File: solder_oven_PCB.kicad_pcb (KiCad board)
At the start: 2 copper layers, 4 parts

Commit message: update: now the pcb has sheets and pcb layout
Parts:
- added B1: ~, JuanDavid_Library:SW-SMD_L3.9-W2.9-LS4.8, F.Cu at (127.1, 104.0)
- added B2: ~, JuanDavid_Library:SW-SMD_L3.9-W2.9-LS4.8, B.Cu at (127.5, 70.9)
- added C1: 100nF, Capacitor_SMD:C_0805_2012Metric, F.Cu at (90.0, 62.3)
- added C2: 1000uF, Capacitor_THT:CP_Radial_D10.0mm_P3.80mm, F.Cu at (142.9, 48.3)
- added C3: 470uF, Capacitor_SMD:C_Elec_8x6.2, B.Cu at (91.0, 82.9)
- added C4: 220uF, Capacitor_SMD:C_Elec_8x6.2, B.Cu at (117.0, 93.9)
- added C5: 100nF, Capacitor_SMD:C_0603_1608Metric, F.Cu at (130.9, 106.5)
- added C6: 100nF, Capacitor_SMD:C_0603_1608Metric, B.Cu at (131.8, 67.9)
- added C7: 100nF, Capacitor_SMD:C_0805_2012Metric, B.Cu at (123.8, 75.0)
- added D1: Generic_Triac_A1A2G, TerminalBlock:TerminalBlock_Altech_AK300-3_P5.00mm, F.Cu at (146.8, 112.0)
- added D2: LED, LED_THT:LED_D3.0mm, B.Cu at (119.4, 120.5)
- added D3: W10G, Diode_THT:Diode_Bridge_Round_D9.8mm, F.Cu at (135.6, 69.2)
- added D4: LED, LED_THT:LED_D3.0mm, F.Cu at (142.1, 59.7)
- added D5: ~, JuanDavid_Library:SMA_L4.4-W2.8-LS5.4-R-RD, B.Cu at (105.0, 76.9)
- added H1: M3 screw, MountingHole:MountingHole_3.2mm_M3_DIN965_Pad, F.Cu at (80.8, 41.9)
- added H2: M3 screw, MountingHole:MountingHole_3.2mm_M3_DIN965_Pad, F.Cu at (149.6, 42.8)
- added H3: M3 screw, MountingHole:MountingHole_3.2mm_M3_DIN965_Pad, F.Cu at (187.3, 137.2)
- added H4: M3 screw, MountingHole:MountingHole_3.2mm_M3_DIN965_Pad, F.Cu at (82.4, 137.0)
- added J1: UART, Connector_PinSocket_2.54mm:PinSocket_1x03_P2.54mm_Vertical, F.Cu at (106.5, 45.2)
- added L1: ~, JuanDavid_Library:IND-SMD_L10.3-W10.3_1274AS-H-330M, B.Cu at (91.0, 95.9)
- added P1: Conn_WallPlug, TerminalBlock_Phoenix:TerminalBlock_Phoenix_MKDS-1,5-2-5.08_1x02_P5.08mm_Horizontal, F.Cu at (148.2, 93.8)
- added R1: Heater, TerminalBlock_Phoenix:TerminalBlock_Phoenix_MKDS-1,5-2-5.08_1x02_P5.08mm_Horizontal, F.Cu at (147.4, 124.5)
- added R10: 3.3K, Resistor_SMD:R_0603_1608Metric, B.Cu at (131.8, 65.0)
- added R11: 1K, Resistor_THT:R_Axial_DIN0204_L3.6mm_D1.6mm_P5.08mm_Horizontal, B.Cu at (111.8, 115.7)
- added R2: 220, Resistor_THT:R_Axial_DIN0204_L3.6mm_D1.6mm_P5.08mm_Horizontal, B.Cu at (122.9, 115.7)
- added R3: 1K, Resistor_THT:R_Axial_DIN0204_L3.6mm_D1.6mm_P5.08mm_Horizontal, B.Cu at (123.1, 106.2)
- added R4: 1M, Resistor_THT:R_Axial_DIN0204_L3.6mm_D1.6mm_P5.08mm_Horizontal, B.Cu at (106.8, 101.5)
- added R5: 10K, Resistor_THT:R_Axial_DIN0204_L3.6mm_D1.6mm_P5.08mm_Horizontal, B.Cu at (102.8, 113.8)
- added R6: 10K, Resistor_THT:R_Axial_DIN0204_L3.6mm_D1.6mm_P5.08mm_Horizontal, F.Cu at (134.8, 55.7)
- added R7: 10K, Resistor_THT:R_Axial_DIN0204_L3.6mm_D1.6mm_P5.08mm_Horizontal, B.Cu at (112.0, 81.6)
- added R8: 3.3K, Resistor_THT:R_Axial_DIN0204_L3.6mm_D1.6mm_P5.08mm_Horizontal, B.Cu at (116.5, 86.7)
- added R9: 3.3K, Resistor_SMD:R_0603_1608Metric, F.Cu at (130.9, 109.5)
- added T2: ~, JuanDavid_Library:AT-010-V, B.Cu at (138.6, 70.6)
- added TC1: Thermocouple, TerminalBlock_Phoenix:TerminalBlock_Phoenix_MKDS-1,5-2-5.08_1x02_P5.08mm_Horizontal, F.Cu at (147.4, 136.1)
- added U4: H11AA1, Package_DIP:DIP-6_W7.62mm, B.Cu at (114.3, 106.2)
- added U5: MOC3052M, Package_DIP:DIP-6_W7.62mm, B.Cu at (114.3, 120.7)
- added U6: ~, JuanDavid_Library:TO-263-5_L10.2-W8.9-P1.70-BR, B.Cu at (104.0, 87.4)
- added U7: ~, JuanDavid_Library:DIP-16_L20.3-W10.2-P2.54-LS10.2-BL, B.Cu at (93.8, 117.5)
- U3: moved to B.Cu
- moved U2 57.9 mm to (90.8, 68.5), turned to 180 degrees
- moved U1 48.6 mm to (112.2, 61.4)
- moved U3 31.1 mm to (117.2, 76.2)
- moved T1 9.18 mm to (108.5, 133.7)
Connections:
- T1 pad 1: unconnected-(T1-VCC-Pad1) -> +5V
- T1 pad 10: unconnected-(T1-T_CLK-Pad10) -> /esp32/T_CLK
- T1 pad 11: unconnected-(T1-T_CS-Pad11) -> /esp32/T_CS
- T1 pad 12: unconnected-(T1-T_DIN-Pad12) -> /esp32/T_DIN
- T1 pad 13: unconnected-(T1-T_DO-Pad13) -> /esp32/T_DO
- T1 pad 14: unconnected-(T1-T_IRQ-Pad14) -> /esp32/T_IRQ
- T1 pad 2: unconnected-(T1-GND-Pad2) -> GND
- T1 pad 3: unconnected-(T1-CS-Pad3) -> /esp32/CS
- T1 pad 4: unconnected-(T1-RST-Pad4) -> /esp32/RST
- T1 pad 5: unconnected-(T1-DC-Pad5) -> /esp32/D/C
- T1 pad 6: unconnected-(T1-MOSI-Pad6) -> /esp32/MOSI
- T1 pad 7: unconnected-(T1-SCK-Pad7) -> /esp32/CLK
- T1 pad 8: unconnected-(T1-LED-Pad8) -> /esp32/LED
- T1 pad 9: unconnected-(T1-MISO-Pad9) -> /esp32/MISO
- U1 pad 1: Net-(U1-GND-Pad1) -> GND
- U1 pad 10: unconnected-(U1-IO25-Pad10) -> /esp32/T_CLK
- U1 pad 13: unconnected-(U1-IO14-Pad13) -> /esp32/CLK
- U1 pad 14: unconnected-(U1-IO12-Pad14) -> /esp32/MISO
- U1 pad 15: unconnected-(U1-GND-Pad15) -> GND
- U1 pad 16: unconnected-(U1-IO13-Pad16) -> /esp32/MOSI
- U1 pad 2: unconnected-(U1-3V3-Pad2) -> +3.3V
- U1 pad 23: unconnected-(U1-IO15-Pad23) -> /esp32/CS
- U1 pad 24: unconnected-(U1-IO2-Pad24) -> /esp32/D/C
- U1 pad 25: unconnected-(U1-IO0-Pad25) -> /esp32/Boot
- U1 pad 26: unconnected-(U1-IO4-Pad26) -> /esp32/D0
- U1 pad 27: unconnected-(U1-IO16-Pad27) -> /trigger_Gate
- U1 pad 29: unconnected-(U1-IO5-Pad29) -> /esp32/RST
- U1 pad 3: unconnected-(U1-EN-Pad3) -> /esp32/EN
- U1 pad 30: unconnected-(U1-IO18-Pad30) -> /esp32/CS_{T}
- U1 pad 33: unconnected-(U1-IO21-Pad33) -> /esp32/LED
- U1 pad 34: unconnected-(U1-RXD0-Pad34) -> /esp32/Tx
- U1 pad 35: unconnected-(U1-TXD0-Pad35) -> /esp32/Rx
- U1 pad 36: unconnected-(U1-IO22-Pad36) -> /esp32/SCK
- U1 pad 38: unconnected-(U1-GND-Pad38) -> GND
- U1 pad 39: Net-(U1-GND-Pad1) -> GND
- U1 pad 4: unconnected-(U1-SENSOR_VP-Pad4) -> /esp32/T_IRQ
- U1 pad 5: unconnected-(U1-SENSOR_VN-Pad5) -> /esp32/T_DO
- U1 pad 6: unconnected-(U1-IO34-Pad6) -> /Zero_Cross
- U1 pad 8: unconnected-(U1-IO32-Pad8) -> /esp32/T_DIN
- U1 pad 9: unconnected-(U1-IO33-Pad9) -> /esp32/T_CS
- U2 pad 1: unconnected-(U2-GND-Pad1) -> GND
- U2 pad 2: unconnected-(U2-T--Pad2) -> GND
- U2 pad 3: unconnected-(U2-T+-Pad3) -> Net-(TC1-+)
- U2 pad 4: unconnected-(U2-VCC-Pad4) -> +3.3V
- U2 pad 5: unconnected-(U2-SCK-Pad5) -> /esp32/SCK
- U2 pad 6: unconnected-(U2-~{CS}-Pad6) -> /esp32/CS_{T}
- U2 pad 7: unconnected-(U2-SO-Pad7) -> /esp32/D0
- U3 pad 1: unconnected-(U3-GND-Pad1) -> GND
- U3 pad 2: Net-(U3-VOUT-Pad2) -> +3.3V
- U3 pad 3: unconnected-(U3-VIN-Pad3) -> +5V
- U3 pad 4: Net-(U3-VOUT-Pad2) -> +3.3V
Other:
- board outline added: 76.8 x 102.7 mm
- board text added: "T_{+}"
- board text added: "T_{-}"

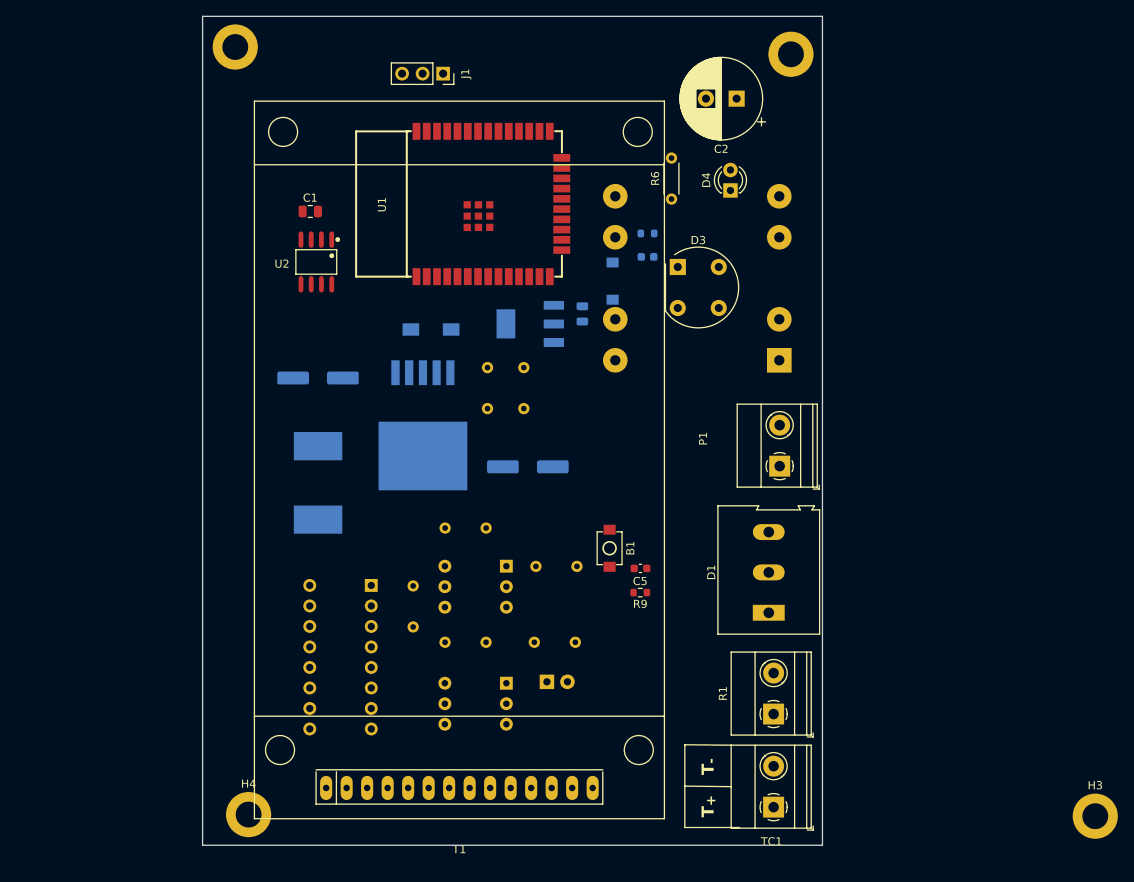
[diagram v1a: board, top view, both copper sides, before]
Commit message: update: pcb with component in place
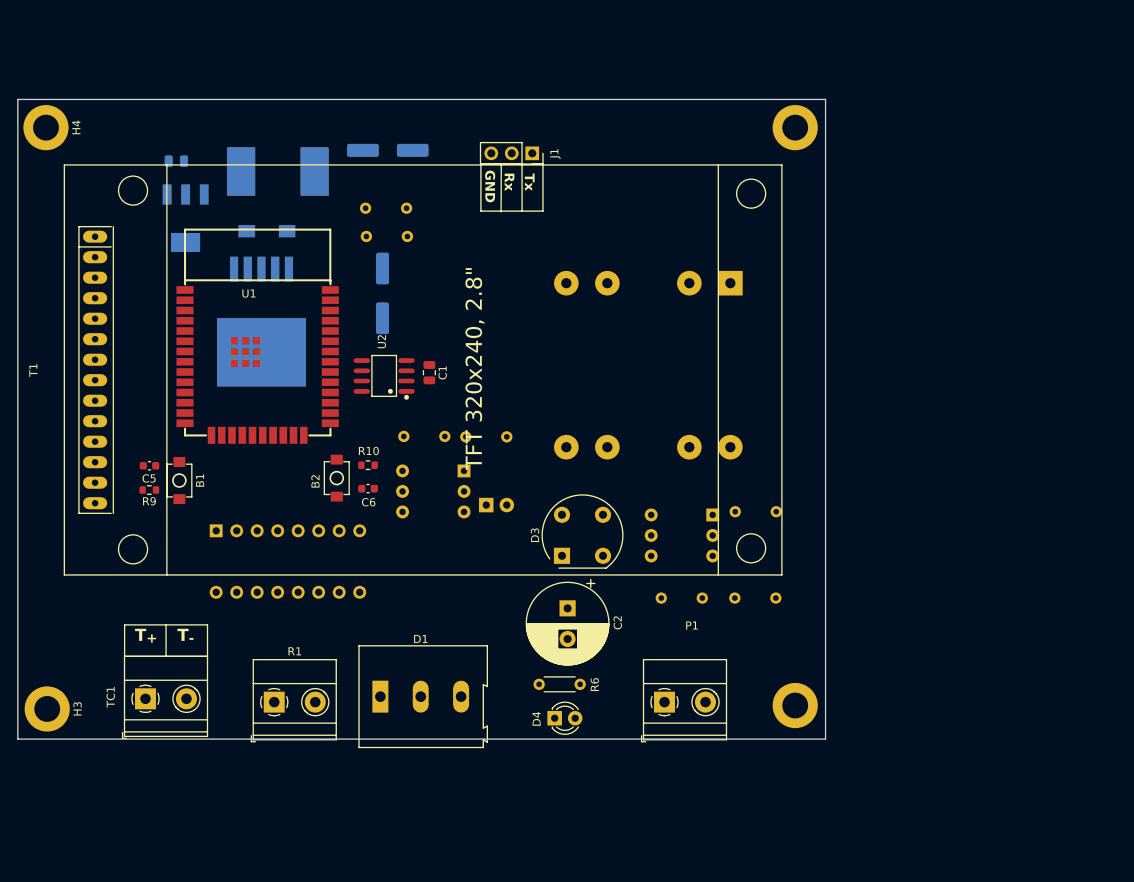
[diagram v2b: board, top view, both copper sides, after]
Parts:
- B2, C6, R10: moved to F.Cu
- moved H3 130.5 mm to (57.5, 123.9), turned to -90 degrees
- moved H4 88.7 mm to (57.3, 51.9), turned to -90 degrees
- moved H2 80.7 mm to (150.1, 123.5), turned to -90 degrees
- moved TC1 79.0 mm to (69.6, 122.7), turned to 0 degrees
- moved H1 70.1 mm to (150.1, 51.9), turned to -90 degrees
- moved D4 68.9 mm to (120.3, 125.1), turned to 0 degrees
- moved T1 68.7 mm to (63.4, 81.9), turned to -90 degrees
- moved C2 66.5 mm to (121.9, 111.4), turned to -90 degrees
- moved R6 66.2 mm to (123.5, 120.9), turned to 180 degrees
- moved R9 62.1 mm to (70.1, 96.8)
- moved C5 62.1 mm to (70.1, 93.8)
- moved R1 61.9 mm to (85.6, 123.1), turned to 0 degrees
- moved B1 54.0 mm to (73.8, 95.6)
- moved C7 53.7 mm to (73.5, 56.0), turned to 180 degrees
- moved D1 49.2 mm to (98.7, 122.4), turned to 0 degrees
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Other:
- board size 76.8 x 102.7 mm -> 100.1 x 79.2 mm
- board text added: "GND"
- board text added: "Rx"
- board text added: "Tx"

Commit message: update: pcb almost done
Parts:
- C2: moved to B.Cu
- moved R3 15.1 mm to (132.8, 97.3), turned to 0 degrees
- moved D4 8.07 mm to (127.2, 120.8), turned to 180 degrees
- moved R6 3.08 mm to (120.4, 120.9)
- moved U4 1.14 mm to (139.7, 101.0)
- moved C3 1.05 mm to (100.0, 72.1)
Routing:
- net +3.3V: track 0.00 -> 263.8 mm, vias 0 -> 9
- net Fase: track 0.00 -> 129.2 mm
- net Neutro: track 0.00 -> 122.7 mm
- net +12v: track 0.00 -> 97.8 mm, vias 0 -> 1
- net Net-(U7-A): track 0.00 -> 74.9 mm, vias 0 -> 6
- net +5V: track 0.00 -> 71.6 mm, vias 0 -> 1
- net Net-(TC1-+): track 0.00 -> 67.8 mm
- net GND: track 0.00 -> 54.4 mm, vias 0 -> 41
- net /esp32/CS: track 0.00 -> 42.0 mm
- net /esp32/D/C: track 0.00 -> 40.1 mm, vias 0 -> 4
- net /esp32/RST: track 0.00 -> 38.1 mm, vias 0 -> 2
- net /esp32/Tx: track 0.00 -> 37.9 mm, vias 0 -> 2
- net 12_{NN}: track 0.00 -> 35.3 mm
- net /esp32/Rx: track 0.00 -> 35.1 mm, vias 0 -> 2
- net /esp32/EN: track 0.00 -> 34.7 mm, vias 0 -> 2
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- added copper zone on B.Cu, net GND
- added copper zone on In2.Cu, net GND
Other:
- copper layers 2 -> 4
